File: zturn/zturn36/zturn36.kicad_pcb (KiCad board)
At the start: 4 copper layers, 189.9 x 136.5 mm, 66 parts, among them J11 Conn_02x40_Odd_Even, J12 Conn_02x40_Odd_Even, J5V1 Conn_01x03, U1 74AXP4T245, U10 74AXP4T245, U11 74AXP4T245, U12 74AXP4T245, U13 74AXP4T245, U14 LM3940_TO220, U2 74AXP4T245, U3 74AXP4T245, U4 74AXP4T245, U5 74AXP4T245, U6 74AXP4T245, U7 74AXP4T245, U8 74AXP4T245, U9 74AXP4T245

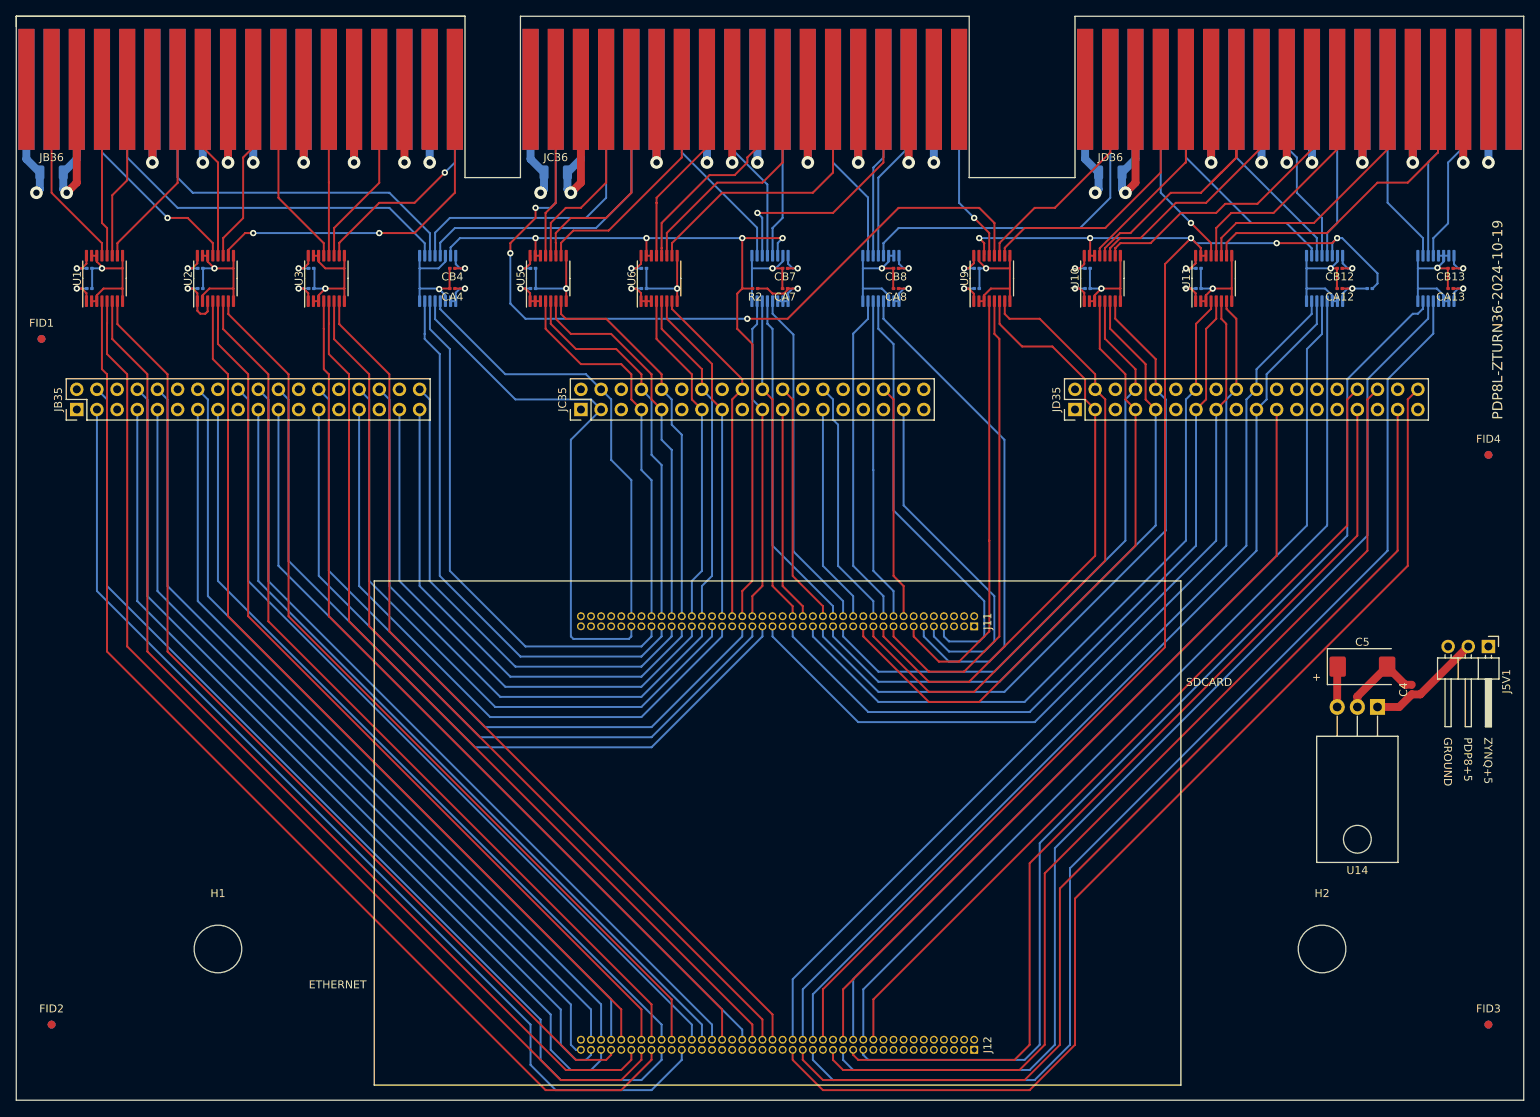
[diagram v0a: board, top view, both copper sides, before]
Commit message: use transistors for bus drivers instead of chips
to handle the 180 & 220-ohm pullups
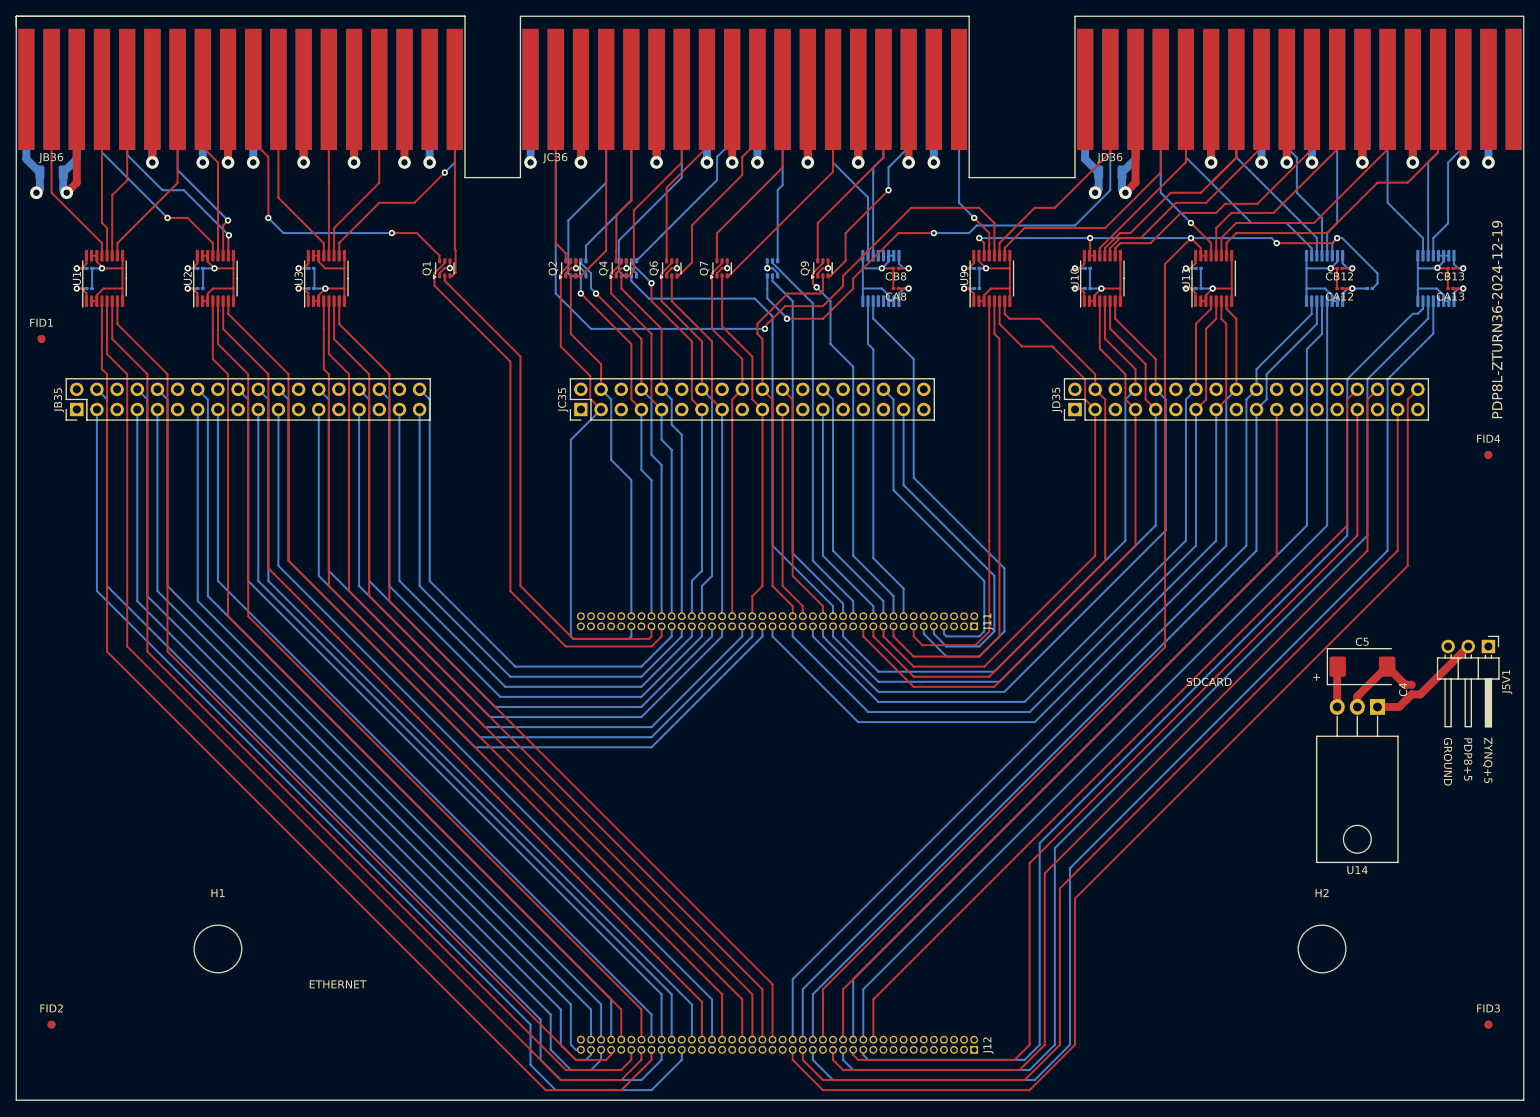
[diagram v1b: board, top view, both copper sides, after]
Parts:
- removed C2: 10u, Capacitor_SMD:C_1206_3216Metric
- removed CA4, CA5, CA6, CA7, CB4, CB5, CB6, CB7: 0.1u, Capacitor_SMD:C_0201_0603Metric
- removed R2: 10K, Resistor_SMD:R_0201_0603Metric
- removed U4, U5, U6, U7: 74AXP4T245, Package_SO:TSSOP-16_4.4x5mm_P0.65mm
- added Q1: SSM6N15AFU, Package_TO_SOT_SMD:SOT-363_SC-70-6, F.Cu at (54.0, 31.8)
- added Q2: SSM6N15AFU, Package_TO_SOT_SMD:SOT-363_SC-70-6, F.Cu at (69.8, 31.8)
- added Q3: SSM6N15AFU, Package_TO_SOT_SMD:SOT-363_SC-70-6, B.Cu at (71.1, 31.7)
- added Q4: SSM6N15AFU, Package_TO_SOT_SMD:SOT-363_SC-70-6, F.Cu at (76.2, 31.8)
- added Q5: SSM6N15AFU, Package_TO_SOT_SMD:SOT-363_SC-70-6, B.Cu at (77.5, 31.8)
- added Q6: SSM6N15AFU, Package_TO_SOT_SMD:SOT-363_SC-70-6, F.Cu at (82.6, 31.8)
- added Q7: SSM6N15AFU, Package_TO_SOT_SMD:SOT-363_SC-70-6, F.Cu at (88.9, 31.8)
- added Q8: SSM6N15AFU, Package_TO_SOT_SMD:SOT-363_SC-70-6, B.Cu at (95.2, 31.8)
- added Q9: SSM6N15AFU, Package_TO_SOT_SMD:SOT-363_SC-70-6, F.Cu at (101.6, 31.8)
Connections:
- J11 pad 11: /iD36B2 -> /o_ADDR_ACCEPT
- J11 pad 16: /oD35B2 -> /oB_BREAK
- J11 pad 18: /o_ADDR_ACCEPT -> /iMEMINCR
- J11 pad 20: /oB_BREAK -> /i_EXTDMAADD_12
- J11 pad 22: /i_EXTDMAADD_12 -> /iCA_INCREMENT
- J11 pad 26: /iCA_INCREMENT -> /iD36B2
- J11 pad 63: /oJMP_JMS -> /iB36V1
- J11 pad 65: /o_KEY_LOAD -> /i_INT_INHIBIT
- J11 pad 7: /iMEMINCR -> /oD35B2
- J12 pad 48: /x_MEM -> /o_LOAD_SF
- J12 pad 52: /o_LOAD_SF -> /oJMP_JMS
- J12 pad 54: /MEMBUSN -> /x_MEM
- J12 pad 56: /MEMBUSF -> /o_KEY_LOAD
- J12 pad 58: /MEMBUSM -> /MEMBUSN
- J12 pad 62: /iB36V1 -> /MEMBUSF
- J12 pad 64: /MEMBUSE -> /MEMBUSM
- J12 pad 66: /i_INT_INHIBIT -> /MEMBUSE
- U2 pad 10: /jB36V1 -> /pJMP_JMS
- U2 pad 11: /j_INT_INHIBIT -> /p_KEY_LOAD
- U2 pad 3: +3V3 -> GND
- U2 pad 6: /i_INT_INHIBIT -> /o_KEY_LOAD
- U2 pad 7: /iB36V1 -> /oJMP_JMS
- U8 pad 12: /jMEMINCR -> unconnected-(U8-1B2-Pad12)
- U8 pad 13: /jD36B2 -> unconnected-(U8-1B1-Pad13)
- U8 pad 2: +3V3 -> GND
- U8 pad 4: /iD36B2 -> unconnected-(U8-1A1-Pad4)
- U8 pad 5: /iMEMINCR -> unconnected-(U8-1A2-Pad5)
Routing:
- net /x_DMAADDR: track 102.0 -> 0.00 mm, vias 4 -> 0
- net /o_KEY_LOAD: track 66.1 -> 118.0 mm
- net /i_INT_INHIBIT: track 115.4 -> 63.7 mm
- net /oJMP_JMS: track 69.9 -> 118.8 mm
- net /iB36V1: track 116.2 -> 69.8 mm
- net GND: track 519.3 -> 479.5 mm, vias 40 -> 43
- net +3V3: track 75.9 -> 47.2 mm, vias 13 -> 9
- net /o_ADDR_ACCEPT: track 40.7 -> 62.0 mm
- net /p_KEY_LOAD: track 45.1 -> 23.8 mm, vias 0 -> 1
- net /jD36B2: track 46.2 -> 67.4 mm, vias 0 -> 2
- net /jB36V1: track 45.3 -> 24.2 mm, vias 2 -> 0
- net /pJMP_JMS: track 48.6 -> 27.8 mm, vias 0 -> 1
- net +5V: track 156.6 -> 136.9 mm, vias 16 -> 12
- net /j_INT_INHIBIT: track 15.2 -> 34.5 mm, vias 0 -> 2
- net /i_BRK_RQST: track 43.1 -> 61.2 mm
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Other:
- board text added: "PDP8L-ZTURN36-2024-12-19"
- board text removed: "PDP8L-ZTURN36-2024-10-19"

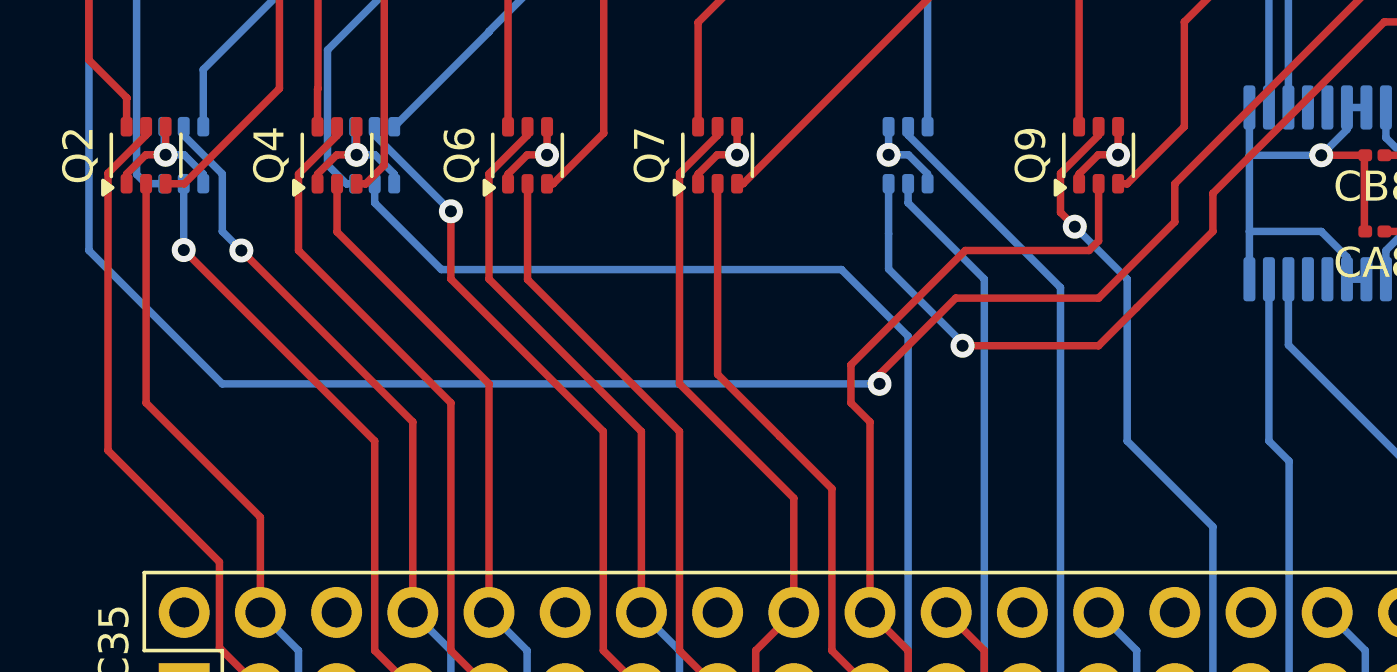
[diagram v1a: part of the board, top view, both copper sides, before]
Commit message: update net names on zturn pcbs to match active high/low signal type
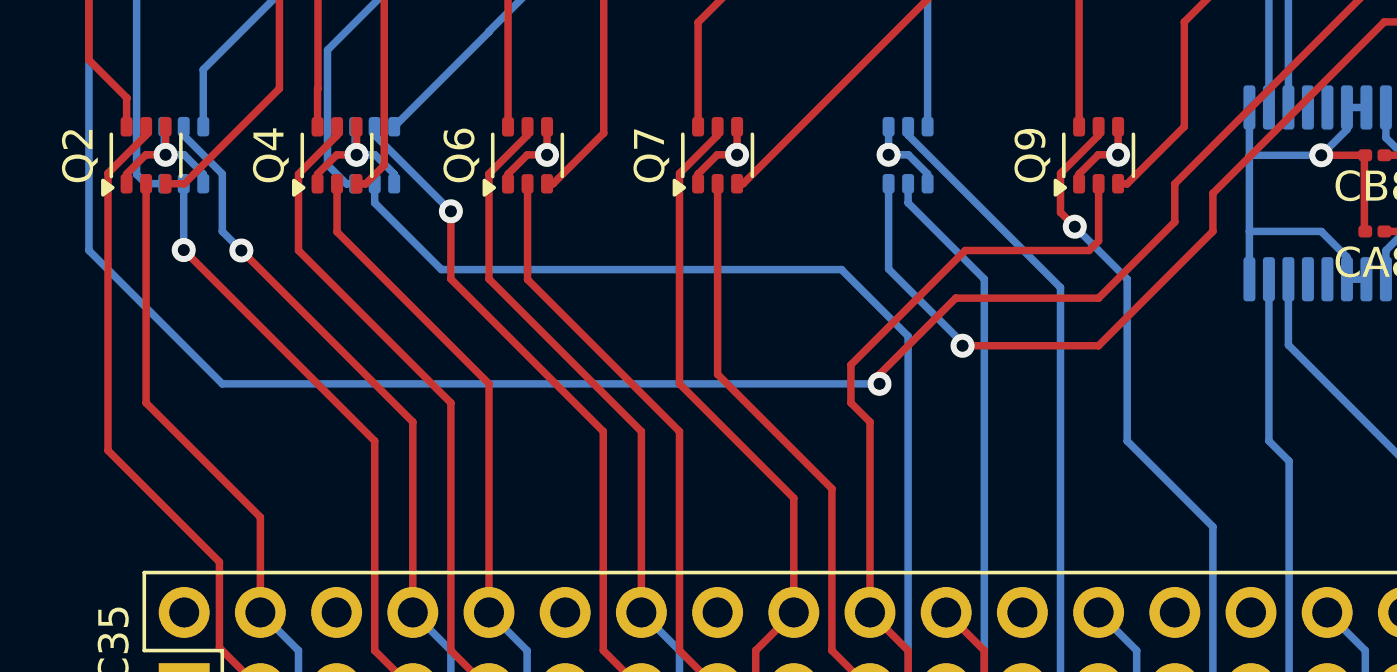
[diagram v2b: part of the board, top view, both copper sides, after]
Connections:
- net /_rBMB renamed /r_BMB
- net /_rMA renamed /r_MA
- net /_xINPUTBUS renamed /x_INPUTBUS
- net /iBEMA renamed /i_BEMA
- net /iMEM07 renamed /iMEM_07
- net /iMEMINCR renamed /i_MEMINCR
- net /iTHREECYCLE renamed /i_3CYCLE
- net /i_INT_RQST renamed /iINT_RQST
- net /jMEMINCR renamed /j_MEMINCR
- net /oBWC_OVERFLOW renamed /o_BWC_OVERFLOW
- net /oB_BREAK renamed /o_B_BREAK
- net /o_BUSINIT renamed /oBUSINIT
- net /pB_BREAK renamed /p_B_BREAK
- net /p_BUSINIT renamed /pBUSINIT

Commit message: update software and further updates to firmware/pcbs
...for invertering transistors

./z8lsimtest works
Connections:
- net /iB36V1 renamed /i_B36V1
- net /iCA_INCREMENT renamed /i_CA_INCRMNT
- net /iD36B2 renamed /i_D36B2
- net /iDATA_IN renamed /i_DATA_IN
- net /iMEM_07 renamed /i_MEM_07
- net /i_3CYCLE renamed /i3CYCLE
- net /i_AC_CLEAR renamed /iAC_CLEAR
- net /i_BEMA renamed /iBEMA
- net /i_BRK_RQST renamed /iBRK_RQST
- net /i_EMA renamed /iEMA
- net /i_EXTDMAADD_12 renamed /iEXTDMAADD_12
- net /i_INT_INHIBIT renamed /iINT_INHIBIT
- net /i_IO_SKIP renamed /iIO_SKIP
- net /i_MEMINCR renamed /iMEMINCR
- net /o_B_RUN renamed /oB_RUN

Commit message: fixed polarity of bus signals for the open-drain transistors
    PDP         Zynq
    MEM         _MEM
    MEM_P       _MEM_P
    _DMAADDR    DMAADDR
    _DMADATA    DMADATA
    _INPUTBUS   INPUTBUS

Also fixed MEMINCR polarity and fixed missing ground connection on circuit board.
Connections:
- net /iMEMINCR renamed /i_MEMINCR
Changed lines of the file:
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@@
   (net 29 "/i_DATA_IN")
   (net 30 "/o_B_BREAK")
-  (net 31 "/iMEMINCR")
+  (net 31 "/i_MEMINCR")
   (net 32 "unconnected-(JD36-PadU1)")
   (net 33 "unconnected-(JD36-PadV1)")
@@
       (net 24 "GND") (pinfunction "S2") (pintype "passive"))
     (pad "5" smd roundrect (at 0.95 0 90) (size 0.65 0.4) (layers "F.Cu" "F.Paste" "F.Mask") (roundrect_rratio 0.25)
-      (net 31 "/iMEMINCR") (pinfunction "G2") (pintype "passive"))
+      (net 31 "/i_MEMINCR") (pinfunction "G2") (pintype "passive"))
     (pad "6" smd roundrect (at 0.95 -0.65 90) (size 0.65 0.4) (layers "F.Cu" "F.Paste" "F.Mask") (roundrect_rratio 0.25)
       (net 75 "/j_DMAADDR_08") (pinfunction "D1") (pintype "passive"))
@@
       (net 194 "/oC36B2") (pinfunction "Pin_17") (pintype "passive"))
     (pad "18" thru_hole oval (at 1.27 -10.16 90) (size 1 1) (drill 0.65) (layers "*.Cu" "*.Mask")
-      (net 31 "/iMEMINCR") (pinfunction "Pin_18") (pintype "passive"))
+      (net 31 "/i_MEMINCR") (pinfunction "Pin_18") (pintype "passive"))
     (pad "19" thru_hole oval (at 0 -11.43 90) (size 1 1) (drill 0.65) (layers "*.Cu" "*.Mask")
       (net 129 "/PIOBUSA") (pinfunction "Pin_19") (pintype "passive"))
